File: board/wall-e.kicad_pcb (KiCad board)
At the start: 2 copper layers, 88.2 x 64.4 mm, 115 parts, among them J1 Raspberry_Pi_2_3, J10 PCA9685, J11 VL53L0X, J12 VL53L0X, J13 VL53L0X, J14 MotorDrv2, J15 Motor2, J16 IMU, J17 INA219, J18 INA219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

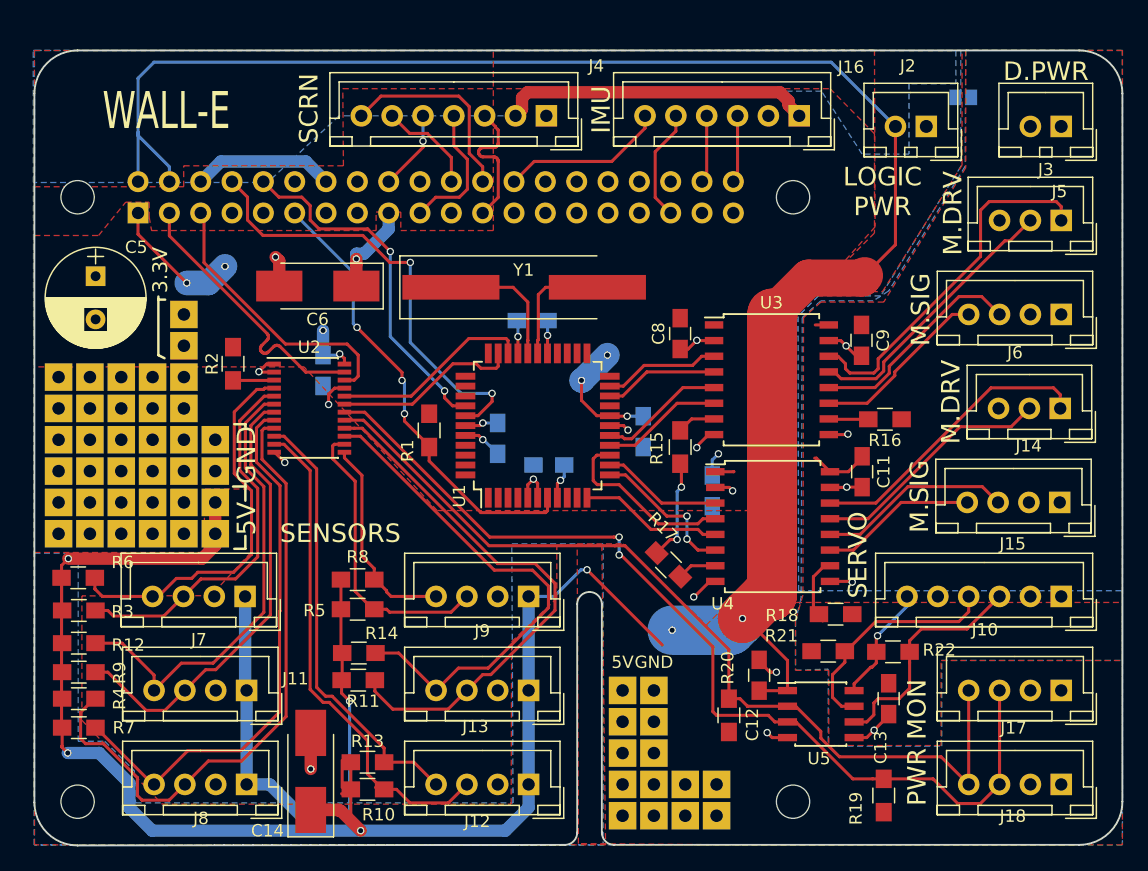
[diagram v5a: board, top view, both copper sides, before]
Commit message: Add 5V cap and tweak.
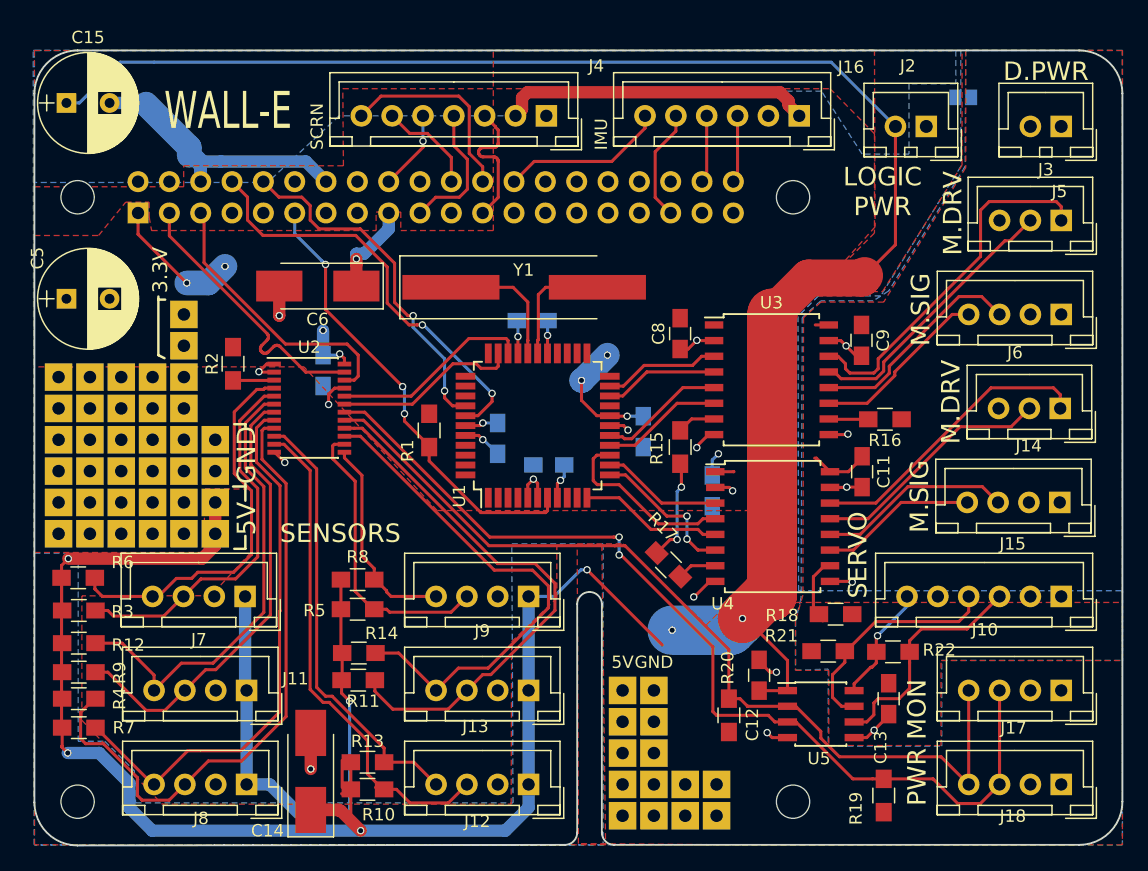
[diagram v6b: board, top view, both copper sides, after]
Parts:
- added C15: 470u, Capacitors_THT:CP_Radial_D8.0mm_P3.50mm, F.Cu at (59.7, 19.1)
- moved C5 2.99 mm to (59.7, 35.0), turned to 0 degrees
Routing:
- net GND: track 45.9 -> 59.5 mm
- net +5V: track 331.2 -> 324.4 mm
- net PI_TX: track 36.4 -> 34.3 mm

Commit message: Tweaks.
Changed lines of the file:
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@@
     (descr "CP, Radial series, Radial, pin pitch=3.50mm, , diameter=8mm, Electrolytic Capacitor")
     (tags "CP Radial series Radial pin pitch 3.50mm  diameter 8mm Electrolytic Capacitor")
-    (fp_text reference C5 (at -2.35 -3.29 90) (layer F.SilkS)
+    (fp_text reference C5 (at -1.645 3.87 90) (layer F.SilkS)
       (effects (font (size 1 1) (thickness 0.15)))
     )
@@
     (descr "CP, Radial series, Radial, pin pitch=3.50mm, , diameter=8mm, Electrolytic Capacitor")
     (tags "CP Radial series Radial pin pitch 3.50mm  diameter 8mm Electrolytic Capacitor")
-    (fp_text reference C15 (at 1.75 -5.31) (layer F.SilkS)
-      (effects (font (size 1 1) (thickness 0.15)))
-    )
+    (fp_text reference C15 (at -1.645 4.295 90) (layer F.SilkS)
+      (effects (font (size 1 1) (thickness 0.15)))
+    )

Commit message: Tweaks.
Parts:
- added J20: GS2, Connectors:GS2, F.Cu at (128.4, 30.7)
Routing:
- net GND: track 59.5 -> 67.5 mm
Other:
- rule via_min_size: 0.4 -> 0.6
- board text added: "V1.0"
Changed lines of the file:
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@@
 (kicad_pcb (version 4) (host pcbnew 4.0.7-e2-6376~61~ubuntu18.04.1)
   (general
-    (links 209)
-    (no_connects 1)
+    (links 211)
+    (no_connects 2)
     (area 57.059999 14.759999 145.410001 79.360001)
     (thickness 1.6)
-    (drawings 82)
-    (tracks 775)
+    (drawings 83)
+    (tracks 777)
     (zones 0)
-    (modules 116)
+    (modules 117)
     (nets 61)
   )
@@
   )
   (setup
-    (last_trace_width 1)
+    (last_trace_width 2)
     (user_trace_width 1)
     (user_trace_width 2)
@@
     (via_size 0.6)
     (via_drill 0.4)
-    (via_min_size 0.4)
+    (via_min_size 0.6)
     (via_min_drill 0.3)
-    (uvia_size 0.3)
+    (uvia_size 0.6)
     (uvia_drill 0.1)
     (uvias_allowed no)
-    (uvia_min_size 0.2)
+    (uvia_min_size 0.6)
     (uvia_min_drill 0.1)
     (pcb_text_width 0.3)
@@
     (via_dia 0.6)
     (via_drill 0.4)
-    (uvia_dia 0.3)
+    (uvia_dia 0.6)
     (uvia_drill 0.1)
     (add_net +3V3)
@@
     )
   )
+  (module Connectors:GS2 (layer F.Cu)
+    (at 128.435 30.735 60)
+    (descr "2-pin solder bridge")
+    (tags "solder bridge")
+    (attr smd)
+    (fp_text reference J20 (at 1.78 0 150) (layer F.SilkS)
+      (effects (font (size 1 1) (thickness 0.15)))
+    )
+    (fp_text value GS2 (at -1.8 0 150) (layer F.Fab)
+      (effects (font (size 1 1) (thickness 0.15)))
+    )
+    (fp_line (start 1.1 -1.45) (end 1.1 1.5) (layer F.CrtYd) (width 0.05))
+    (fp_line (start 1.1 1.5) (end -1.1 1.5) (layer F.CrtYd) (width 0.05))
+    (fp_line (start -1.1 1.5) (end -1.1 -1.45) (layer F.CrtYd) (width 0.05))
+    (fp_line (start -1.1 -1.45) (end 1.1 -1.45) (layer F.CrtYd) (width 0.05))
+    (fp_line (start -0.89 -1.27) (end -0.89 1.27) (layer F.SilkS) (width 0.12))
+    (fp_line (start 0.89 1.27) (end 0.89 -1.27) (layer F.SilkS) (width 0.12))
+    (fp_line (start 0.89 1.27) (end -0.89 1.27) (layer F.SilkS) (width 0.12))
+    (fp_line (start -0.89 -1.27) (end 0.89 -1.27) (layer F.SilkS) (width 0.12))
+    (pad 1 smd rect (at 0 -0.64 60) (size 1.27 0.97) (layers F.Cu F.Paste F.Mask)
+      (net 4 +5V))
+    (pad 2 smd rect (at 0 0.64 60) (size 1.27 0.97) (layers F.Cu F.Paste F.Mask)
+      (net 3 +5VP))
+  )
+  (gr_text V1.0 (at 72.785 21.635) (layer F.SilkS)
+    (effects (font (size 1.5 1.5) (thickness 0.3)))
+  )
   (gr_text GND (at 107.355 64.429) (layer F.SilkS)
     (effects (font (size 1 1) (thickness 0.25)))
@@
     (effects (font (size 1.5 1.5) (thickness 0.3)))
   )
-  (gr_text WALL-E (at 72.835 19.725) (layer F.SilkS)
+  (gr_text WALL-E (at 72.785 18.585) (layer F.SilkS)
     (effects (font (size 3 2) (thickness 0.325)))
   )
@@
   (segment (start 106.485 44.485) (end 105.185 44.485) (width 0.25) (layer B.Cu) (net 1) (status 10))
   (via (at 105.185 44.485) (size 0.6) (drill 0.4) (layers F.Cu B.Cu) (net 1))
-  (segment (start 70.615 25.47) (end 70.615 24.064998) (width 1) (layer B.Cu) (net 2))
-  (segment (start 70.615 24.064998) (end 70.839999 23.839999) (width 1) (layer B.Cu) (net 2))
-  (segment (start 72.245001 23.839999) (end 70.839999 23.839999) (width 1) (layer B.Cu) (net 2))
+  (segment (start 80.775 25.47) (end 80.775 24.267919) (width 2) (layer B.Cu) (net 2))
+  (segment (start 80.775 24.267919) (end 79.592081 23.085) (width 2) (layer B.Cu) (net 2))
+  (segment (start 79.592081 23.085) (end 71.594998 23.085) (width 2) (layer B.Cu) (net 2))
+  (segment (start 71.594998 23.085) (end 70.839999 23.839999) (width 2) (layer B.Cu) (net 2))
+  (segment (start 70.615 25.47) (end 70.615 24.064998) (width 2) (layer B.Cu) (net 2))
+  (segment (start 70.615 24.064998) (end 70.839999 23.839999) (width 2) (layer B.Cu) (net 2))
+  (segment (start 66.09 19.09) (end 70.839999 23.839999) (width 2) (layer B.Cu) (net 2))
+  (segment (start 66.09 19.09) (end 63.23 19.09) (width 2) (layer B.Cu) (net 2))
   (segment (start 70.839999 23.839999) (end 69.682081 22.682081) (width 1) (layer B.Cu) (net 2))
-  (segment (start 63.23 19.09) (end 66.09 19.09) (width 1) (layer B.Cu) (net 2))
   (segment (start 66.09 19.09) (end 66.185 19.185) (width 1) (layer B.Cu) (net 2))
   (segment (start 69.682081 22.682081) (end 66.185 19.185) (width 2) (layer B.Cu) (net 2))
@@
   (segment (start 113.456756 50.256756) (end 113.735 50.535) (width 0.25) (layer F.Cu) (net 2))
   (via (at 113.735 50.535) (size 0.6) (drill 0.4) (layers F.Cu B.Cu) (net 2))
-  (segment (start 72.245001 23.839999) (end 79.144999 23.839999) (width 1) (layer B.Cu) (net 2))
-  (segment (start 79.144999 23.839999) (end 80.775 25.47) (width 1) (layer B.Cu) (net 2) (status 20))
   (segment (start 75.365262 40.910252) (end 75.335 40.87999) (width 0.25) (layer F.Cu) (net 2))
   (segment (start 76.567958 40.910252) (end 75.365262 40.910252) (width 0.25) (layer F.Cu) (net 2) (status 10))
